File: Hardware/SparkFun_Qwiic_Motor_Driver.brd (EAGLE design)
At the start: 25.4 x 25.4 mm, 58 parts, among them U1 CY8C4245LQI-483, U2 DRV8835

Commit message: v01
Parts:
- added U$18: (no value), buzzard_labels (2):QWIIC_MOTOR_DRIVER0
- LOGO3: value SFE_LOGO_NAME_FLAME.1_INCH -> SFE_LOGO_NAME.1_INCH; device SparkFun-Aesthetics:SFE_LOGO_NAME_FLAME_.1 -> SparkFun-Aesthetics:SFE_LOGO_NAME_.1
- moved LOGO3 6.27 mm to (12.7, 12.2)
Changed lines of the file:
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@@
 <layer number="28" name="bValues" color="7" fill="1" visible="no" active="yes"/>
 <layer number="29" name="tStop" color="7" fill="3" visible="no" active="yes"/>
-<layer number="30" name="bStop" color="7" fill="6" visible="no" active="yes"/>
+<layer number="30" name="bStop" color="7" fill="6" visible="yes" active="yes"/>
 <layer number="31" name="tCream" color="7" fill="4" visible="no" active="yes"/>
 <layer number="32" name="bCream" color="7" fill="5" visible="no" active="yes"/>
@@
 </element>
 <element name="LOGO2" library="SparkFun-Aesthetics" package="OSHW-LOGO-MINI" value="OSHW-LOGOMINI" x="21.336" y="17.78" smashed="yes"/>
-<element name="LOGO3" library="SparkFun-Aesthetics" package="SFE_LOGO_NAME_FLAME_.1" value="SFE_LOGO_NAME_FLAME.1_INCH" x="17.78" y="8.509" smashed="yes" rot="MR0"/>
+<element name="LOGO3" library="SparkFun-Aesthetics" package="SFE_LOGO_NAME_.1" value="SFE_LOGO_NAME.1_INCH" x="12.7" y="12.192" smashed="yes" rot="MR0"/>
 <element name="R1" library="SparkFun-Resistors" package="0603" value="1" x="17.399" y="11.1506" smashed="yes">
 <attribute name="NAME" x="17.399" y="11.9126" size="0.6096" layer="25" font="vector" ratio="20" align="bottom-center"/>
@@
 <element name="U$17" library="buzzard_labels (1)" package="PU1" value="" x="3.81" y="9.017" smashed="yes" rot="MR270"/>
 <element name="TP1" library="SparkFun-Connectors" package="TP_15TH" value="RESET" x="3.81" y="13.208" smashed="yes"/>
+<element name="U$18" library="buzzard_labels (2)" package="QWIIC_MOTOR_DRIVER0" value="" x="21.971" y="9.906" smashed="yes" rot="MR0"/>
 </elements>
 <signals>

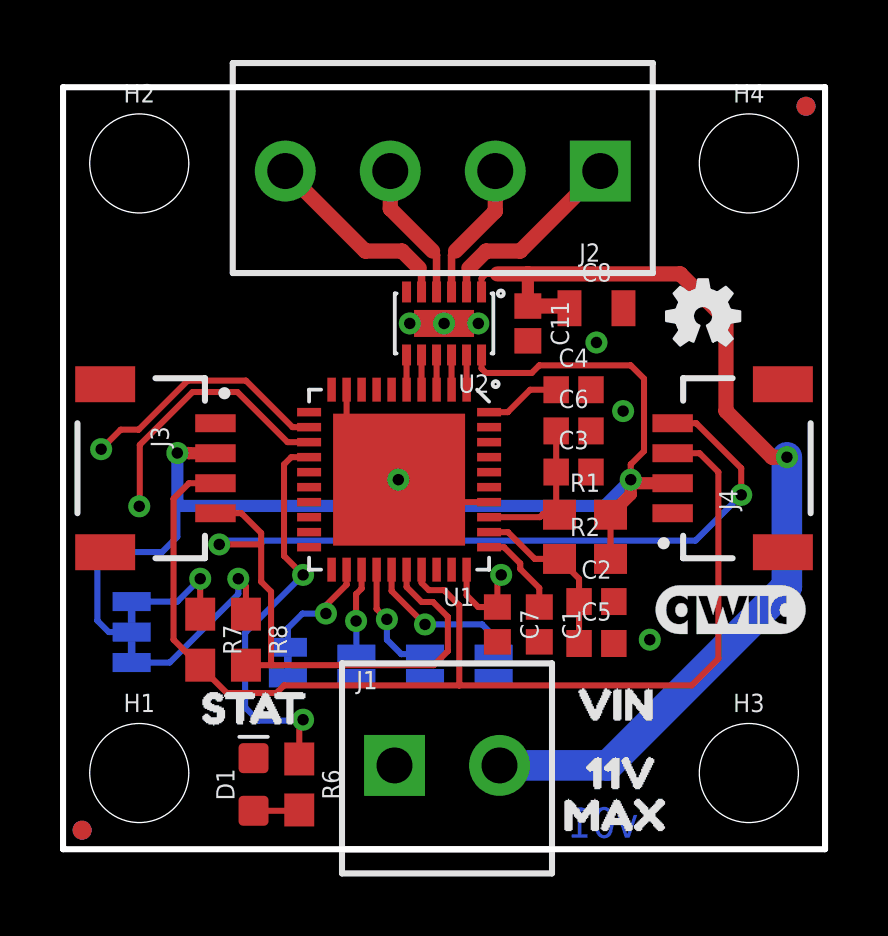
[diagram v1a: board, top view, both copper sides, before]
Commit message: v01 Design Review Changes
- Added I2C test points
- Moved motor connector symbol to connection section
- Changed status LED to blue
- Adjusted VIN trace width
- Added SFE flame to top side of board
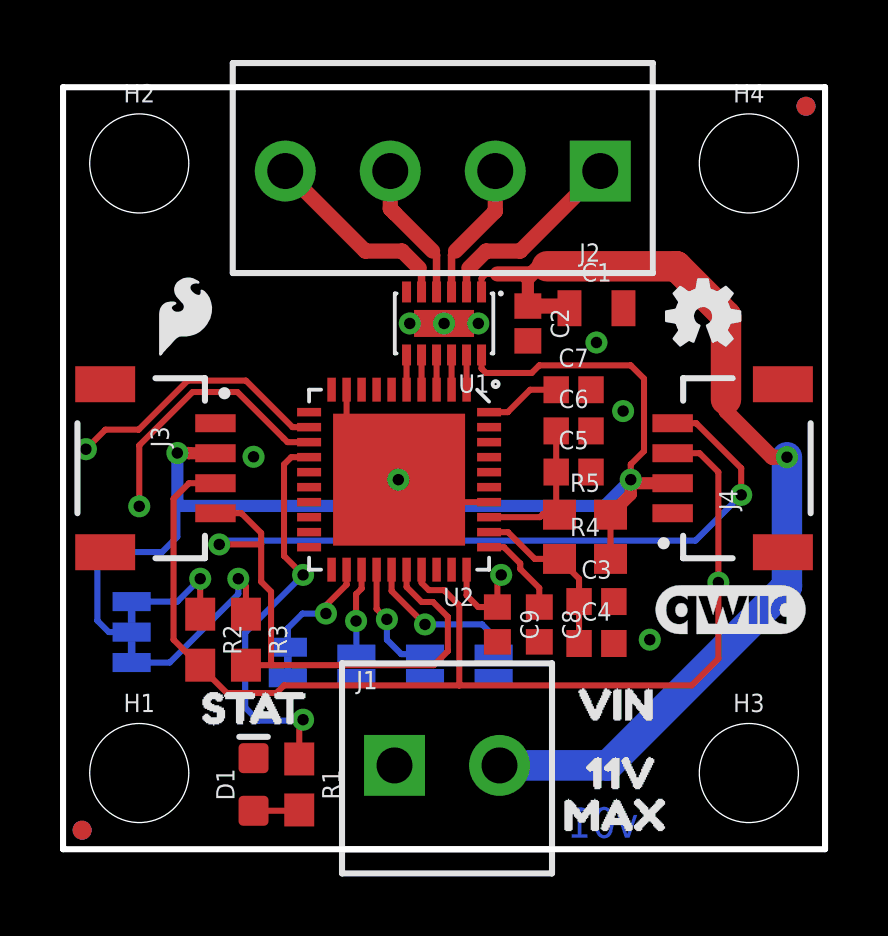
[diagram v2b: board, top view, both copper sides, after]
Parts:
- removed C11: 0.1uF, SparkFun-Capacitors:0402
- removed R6: 470, SparkFun-Resistors:0603
- removed R7: 4.7k, SparkFun-Resistors:0603
- added C9: 0.1uF, SparkFun-Capacitors:0402
- added R4, R5: 1, SparkFun-Resistors:0603
- added TP5, TP6: (no value), SparkFun-Connectors:TP_15TH
- added U$19: (no value), SparkFun-Aesthetics:SFE_LOGO_FLAME_.1
- C1: value 1.0uF -> 10uF; device SparkFun-Capacitors:0402 -> SparkFun-Capacitors:0805
- C2, C4: value 1.0uF -> 0.1uF
- C5, C7: value 0.1uF -> 1.0uF
- C8: value 10uF -> 1.0uF; device SparkFun-Capacitors:0805 -> SparkFun-Capacitors:0402
- D1: value RED -> BLUE
- J1: value (none) -> Power In
- J2: value (none) -> Motor Connections
- J3, J4: value (none) -> Qwiic
- R1: value 1 -> 470
- R2: value 1 -> 4.7k
- TP1, TP4: value RESET -> (none)
- TP2: value SWD_IO -> (none)
- TP3: value SWD_CLK -> (none)
- U1: value CY8C4245LQI-483 -> DRV8835; device PSOC4TempLib:QFN-40 -> SparkFun-IC-Special-Function:WSON-12
- U2: value DRV8835 -> CY8C4245LQI-483; device PSOC4TempLib:WSON-12 -> SparkFun-IC-Microcontroller:QFN-40
- moved R2 13.1 mm to (4.57, 6.99), turned to 270 degrees
- moved R1 13.1 mm to (7.87, 2.16), turned to 270 degrees
- moved C1 10.7 mm to (17.8, 18.0), turned to 0 degrees
- moved C8 10.7 mm to (15.9, 7.49), turned to 270 degrees
- moved C2 9.55 mm to (15.5, 17.5), turned to 270 degrees
- moved C4 8.49 mm to (17.8, 6.86)
- moved C7 8.23 mm to (17.0, 15.3), turned to 0 degrees
- moved C5 5.77 mm to (17.0, 12.6)
- moved U1 5.42 mm to (12.7, 17.5)
- moved U2 5.42 mm to (11.2, 12.3)
- moved C3 4.38 mm to (17.8, 8.26)
- moved TP2 0.51 mm to (0.76, 13.3), flipped to the top
- flipped TP3 to the top
- flipped TP4 to the top
- renumbered R8 to R3
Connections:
- net !RESET: now also C9.1, U2.30; no longer C7.1, U1.30
- net 3.3V: now also R4.2, R5.2, U1.12; no longer R1.2, R2.2, U2.12
- net AOUT1: now also U1.2; no longer U2.2
- net AOUT2: now also U1.3; no longer U2.3
- net BOUT1: now also U1.4; no longer U2.4
- net BOUT2: now also U1.5; no longer U2.5
- net GND: now also C9.2, U1.6, U1.PAD, U2.34, U2.9, U2.EP; no longer C11.2, U1.34, U1.9, U1.EP, U2.6, U2.PAD
- net MODEB0: now also U2.22; no longer U1.22
- net MODEB1: now also U2.23; no longer U1.23
- net MODEB2: now also U2.24; no longer U1.24
- net MODEB3: now also U2.25; no longer U1.25
- net N$1: now also C8.1, U2.31; no longer C1.1, U1.31
- net N$10: now also R1.2; no longer R6.2
- net N$12: now also R2.1; no longer R7.1
- net N$3: now also C5.1, R5.1, U2.33; no longer C3.1, R1.1, U1.33
- net N$4: now also C7.1, U2.40; no longer C4.1, U1.40
- net P2.0: now also U1.11, U2.1; no longer U1.1, U2.11
- net P2.1: now also U1.10, U2.2; no longer U1.2, U2.10
- net P2.2: now also U1.9, U2.3; no longer U1.3, U2.9
- net P2.3: now also U1.8, U2.4; no longer U1.4, U2.8
- net P2.4: now also U1.7, U2.5; no longer U1.5, U2.7
- net P3.2: now also U2.12; no longer U1.12
- net P3.3: now also U2.13; no longer U1.13
- net SCL: now also TP6.P$1, U2.26; no longer U1.26
- net SDA: now also R2.2, TP5.P$1, U2.27; no longer R7.2, U1.27
- net SLED: now also R1.1, U2.14; no longer R6.1, U1.14
- net VDDD: now also C3.1, C4.1, R4.1, U2.32; no longer C2.1, C5.1, R2.1, U1.32
- net VIN: now also C1.1, C2.1, U1.1; no longer C11.1, C8.1, U2.1
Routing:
- net GND: track 8.50 -> 7.05 mm, vias 7 -> 8
- net P3.2: track 8.52 -> 9.03 mm
- net SCL: vias 2 -> 1

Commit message: v10
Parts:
- JP1: device SparkFun-Jumpers:SMT-JUMPER_2_NC_TRACE_NO-SILK -> SparkFun-Jumpers:SMT-JUMPER_2_NO_NO-SILK
- JP4: device SparkFun-Jumpers:SMT-JUMPER_2_NO_NO-SILK -> SparkFun-Jumpers:SMT-JUMPER_2_NC_TRACE_NO-SILK
- moved JP1 0.13 mm to (7.49, 6.10)
- moved JP4 0.13 mm to (14.4, 6.22)
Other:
- board text added: "v10"
- board text removed: "v01"
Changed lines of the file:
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@@
 <layer number="28" name="bValues" color="7" fill="1" visible="no" active="yes"/>
 <layer number="29" name="tStop" color="7" fill="3" visible="no" active="yes"/>
-<layer number="30" name="bStop" color="7" fill="6" visible="yes" active="yes"/>
+<layer number="30" name="bStop" color="7" fill="6" visible="no" active="yes"/>
 <layer number="31" name="tCream" color="7" fill="4" visible="no" active="yes"/>
 <layer number="32" name="bCream" color="7" fill="5" visible="no" active="yes"/>
@@
 <layer number="46" name="Milling" color="3" fill="1" visible="no" active="yes"/>
 <layer number="47" name="Measures" color="7" fill="1" visible="yes" active="yes"/>
-<layer number="48" name="Document" color="7" fill="1" visible="yes" active="yes"/>
+<layer number="48" name="Document" color="7" fill="1" visible="no" active="yes"/>
 <layer number="49" name="Reference" color="7" fill="1" visible="yes" active="yes"/>
 <layer number="50" name="dxf" color="7" fill="1" visible="no" active="no"/>
@@
 <dimension x1="0" y1="0" x2="0" y2="25.4" x3="-6.35" y3="12.7" textsize="1.016" layer="47" unit="inch"/>
 <dimension x1="0" y1="0" x2="25.4" y2="0" x3="12.7" y3="-11.43" textsize="1.016" layer="47" unit="inch" visible="yes"/>
-<text x="19.177" y="0.381" size="1.016" layer="16" font="vector" ratio="20" rot="SMR0">v01</text>
+<text x="19.177" y="0.381" size="1.016" layer="16" font="vector" ratio="20" rot="SMR0">v10</text>
 <text x="19.05" y="-25.4" size="1.778" layer="51" font="vector">Alex Wende</text>
 <wire x1="10.668" y1="2.286" x2="27.178" y2="2.286" width="4.5212" layer="48"/>
@@
 </element>
 <element name="FRAME1" library="SparkFun-Aesthetics" package="CREATIVE_COMMONS" value="FRAME-LETTER" x="-7.747" y="-25.273" smashed="yes"/>
-<element name="JP4" library="SparkFun-Jumpers" package="SMT-JUMPER_2_NO_NO-SILK" value="JUMPER-PAD-2" x="14.351" y="6.096" smashed="yes" rot="MR90">
-<attribute name="NAME" x="15.621" y="5.188" size="0.4064" layer="26" rot="MR90"/>
-<attribute name="VALUE" x="12.7" y="5.188" size="0.4064" layer="28" rot="MR90"/>
+<element name="JP4" library="SparkFun-Jumpers" package="SMT-JUMPER_2_NC_TRACE_NO-SILK" value="JUMPER-PAD-2" x="14.351" y="6.223" smashed="yes" rot="MR90">
+<attribute name="NAME" x="15.621" y="5.315" size="0.4064" layer="26" rot="MR90"/>
+<attribute name="VALUE" x="12.7" y="5.315" size="0.4064" layer="28" rot="MR90"/>
 </element>
 <element name="JP3" library="SparkFun-Jumpers" package="SMT-JUMPER_2_NO_NO-SILK" value="JUMPER-PAD-2" x="12.065" y="6.096" smashed="yes" rot="MR90">
@@
 <attribute name="VALUE" x="8.128" y="5.188" size="0.4064" layer="28" rot="MR90"/>
 </element>
-<element name="JP1" library="SparkFun-Jumpers" package="SMT-JUMPER_2_NC_TRACE_NO-SILK" value="JUMPER-PAD-2" x="7.493" y="6.223" smashed="yes" rot="MR90">
-<attribute name="NAME" x="8.763" y="5.315" size="0.4064" layer="26" rot="MR90"/>
-<attribute name="VALUE" x="5.842" y="5.315" size="0.4064" layer="28" rot="MR90"/>
+<element name="JP1" library="SparkFun-Jumpers" package="SMT-JUMPER_2_NO_NO-SILK" value="JUMPER-PAD-2" x="7.493" y="6.096" smashed="yes" rot="MR90">
+<attribute name="NAME" x="8.763" y="5.188" size="0.4064" layer="26" rot="MR90"/>
+<attribute name="VALUE" x="5.842" y="5.188" size="0.4064" layer="28" rot="MR90"/>
 </element>
 <element name="JP6" library="SparkFun-Jumpers" package="SMT-JUMPER_3_2-NC_TRACE_NO-SILK" value="JUMPER-SMT_3_2-NC_TRACE_NO-SILK" x="2.286" y="7.239" smashed="yes" rot="MR90">
@@
 <wire x1="8.763" y1="7.8566" x2="7.9836" y2="7.8566" width="0.2032" layer="16"/>
 <wire x1="7.9836" y1="7.8566" x2="7.493" y2="7.366" width="0.2032" layer="16"/>
-<wire x1="7.493" y1="7.366" x2="7.493" y2="6.731" width="0.2032" layer="16"/>
+<wire x1="7.493" y1="7.366" x2="7.493" y2="6.5024" width="0.2032" layer="16"/>
 <contactref element="U2" pad="22"/>
 <wire x1="9.4514" y1="9.319" x2="9.4514" y2="8.8164" width="0.2032" layer="1"/>
@@
 <wire x1="12.065" y1="7.493" x2="13.97" y2="7.493" width="0.2032" layer="16"/>
 <wire x1="13.97" y1="7.493" x2="14.351" y2="7.112" width="0.2032" layer="16"/>
-<wire x1="14.351" y1="7.112" x2="14.351" y2="6.5024" width="0.2032" layer="16"/>
+<wire x1="14.351" y1="7.112" x2="14.351" y2="6.731" width="0.2032" layer="16"/>
 <contactref element="U2" pad="25"/>
 <wire x1="10.9514" y1="9.319" x2="10.9514" y2="8.6066" width="0.2032" layer="1"/>
